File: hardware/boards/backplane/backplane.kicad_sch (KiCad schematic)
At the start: 0 parts

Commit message: Starrting to move things around
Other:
- added sheet Slot Connectors (backplane_slot_connectors.kicad_sch)
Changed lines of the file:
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@@
+	)
+	(sheet
+		(at 35.56 101.6)
+		(size 58.42 15.24)
+		(exclude_from_sim no)
+		(in_bom yes)
+		(on_board yes)
+		(dnp no)
+		(fields_autoplaced yes)
+		(stroke
+			(width 0.1524)
+			(type solid)
+		)
+		(fill
+			(color 0 0 0 0)
+		)
+		(property "Sheetname" "Slot Connectors"
+			(at 35.56 100.8884 0)
+			(show_name no)
+			(do_not_autoplace no)
+			(effects
+				(font
+					(size 1.27 1.27)
+				)
+				(justify left bottom)
+			)
+		)
+		(property "Sheetfile" "backplane_slot_connectors.kicad_sch"
+			(at 35.56 117.9446 0)
+			(show_name no)
+			(do_not_autoplace no)
+			(effects
+				(font
+					(size 1.27 1.27)
+				)
+				(justify left top)
+			)
+		)
 	)
 	(sheet

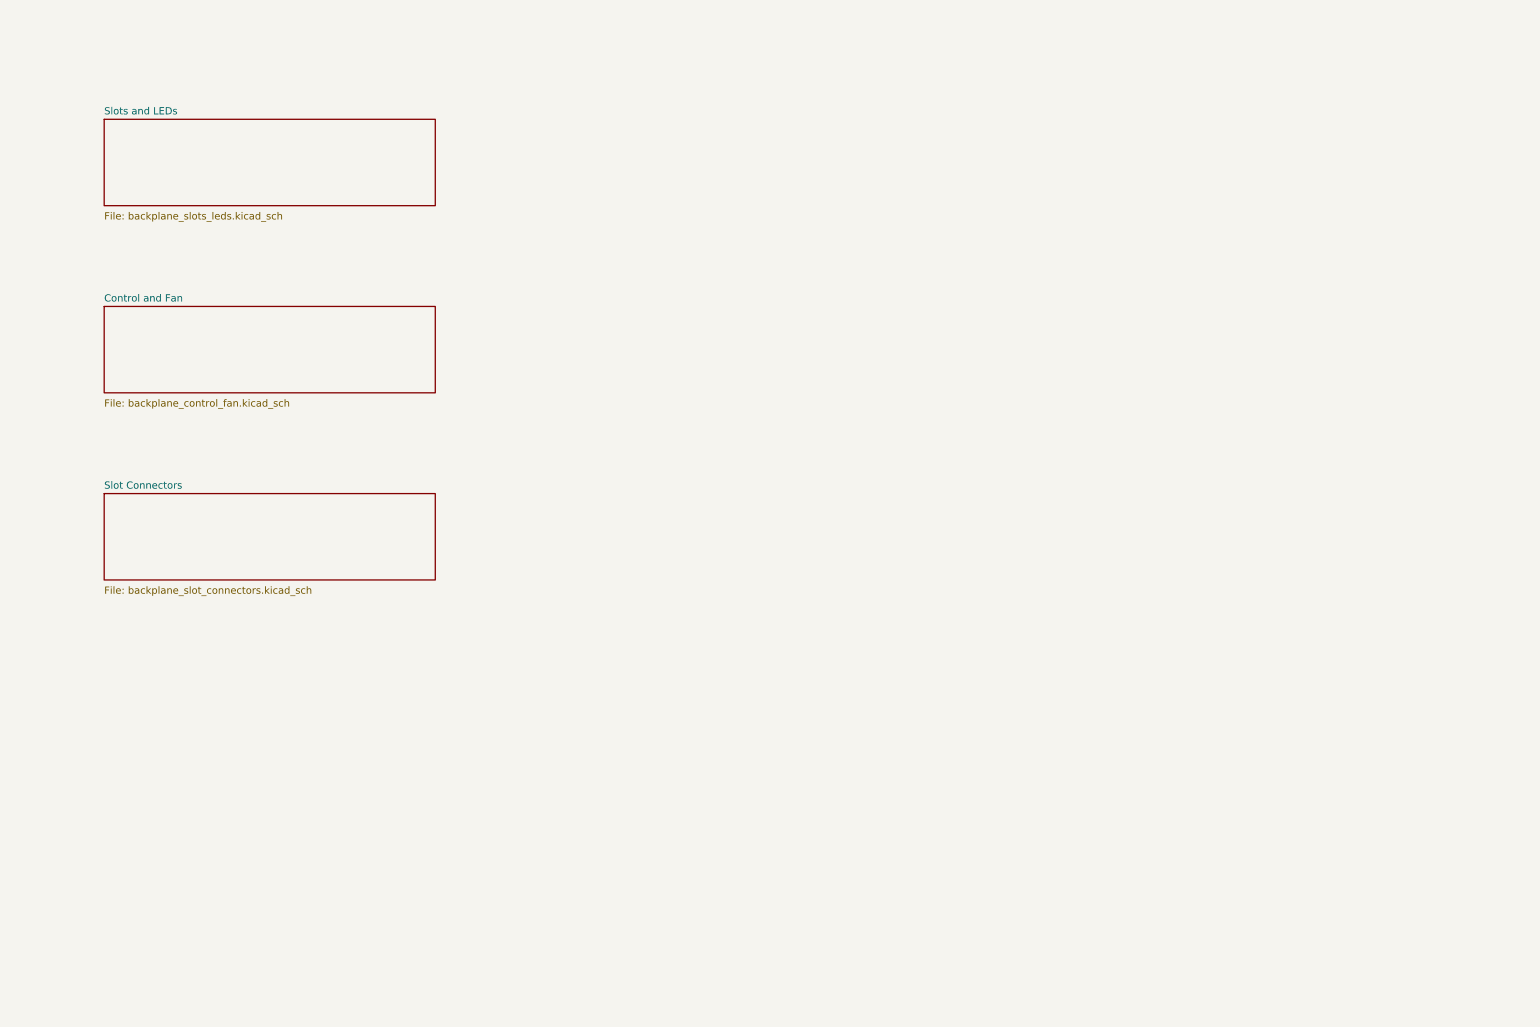
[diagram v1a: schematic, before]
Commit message: Clean up the backplane schematic
And start over with the PCB using a bit saner layout
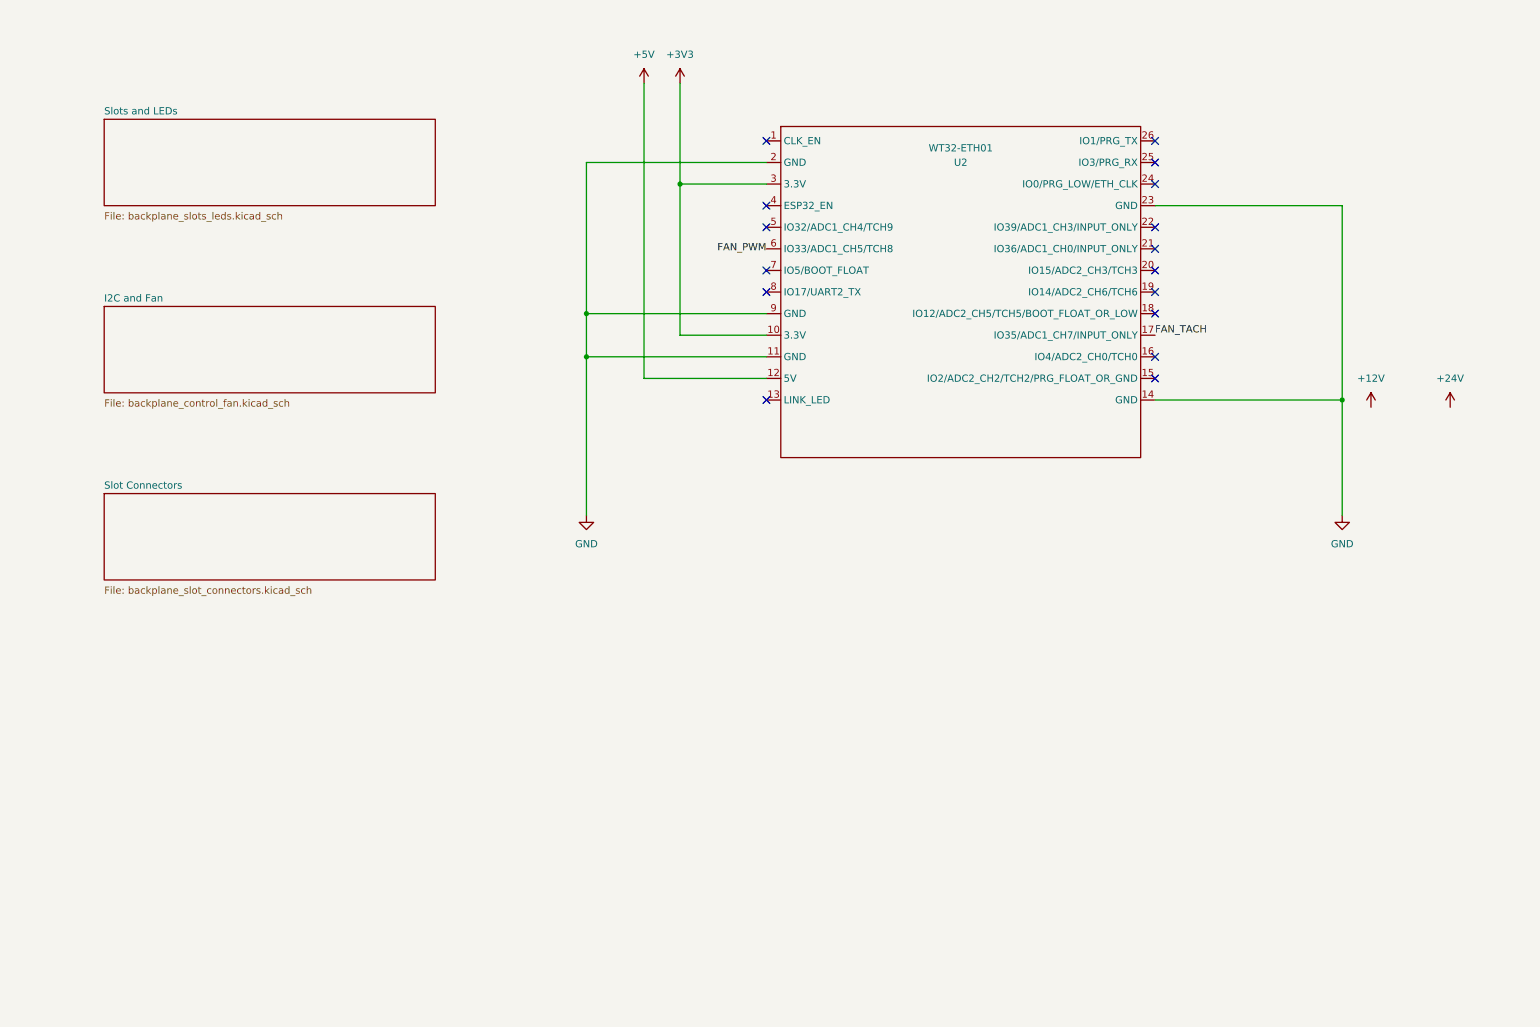
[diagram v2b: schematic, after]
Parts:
- added U2: WT32-ETH01, WT32-ETH01:WT32-ETH01, symbol WT32-ETH01:WT32-ETH01
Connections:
- new net +3V3: U2.10 (3.3V), U2.3 (3.3V)
- new net +5V: U2.12 (5V)
- new net FAN_PWM: U2.6 (IO33/ADC1_CH5/TCH8)
- new net FAN_TACH: U2.17 (IO35/ADC1_CH7/INPUT_ONLY)
- new net GND: U2.11 (GND), U2.14 (GND), U2.2 (GND), U2.23 (GND), U2.9 (GND)
- no-connect marks 0 -> 16
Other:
- sheet Control and Fan renamed I2C and Fan

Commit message: Split controller hardware from backplane
Add the central controller KiCad project for the WT32 and fan circuit, retain the I2C mux on the backplane, and update the system/interface documentation. Use C7519 arrays for interim slot I2C protection and record assembly-part alternatives.
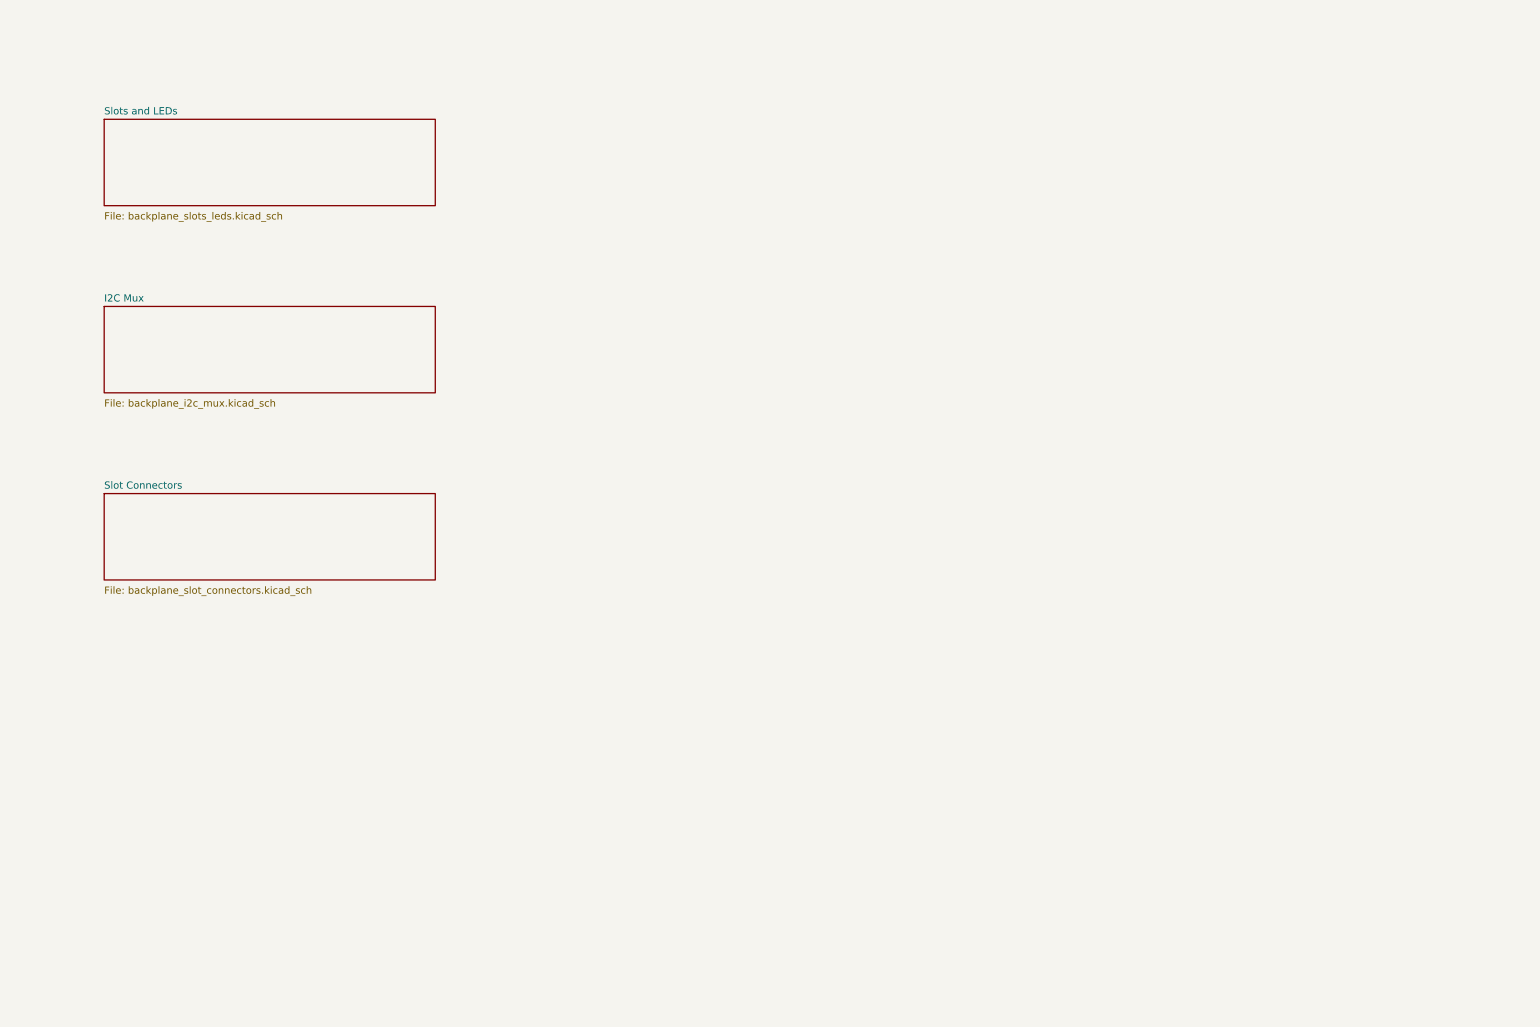
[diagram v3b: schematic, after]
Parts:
- removed U2: WT32-ETH01, WT32-ETH01:WT32-ETH01, symbol WT32-ETH01:WT32-ETH01
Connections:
- no-connect marks 16 -> 0
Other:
- sheet I2C and Fan renamed I2C Mux
- sheet I2C Mux: file backplane_control_fan.kicad_sch -> backplane_i2c_mux.kicad_sch

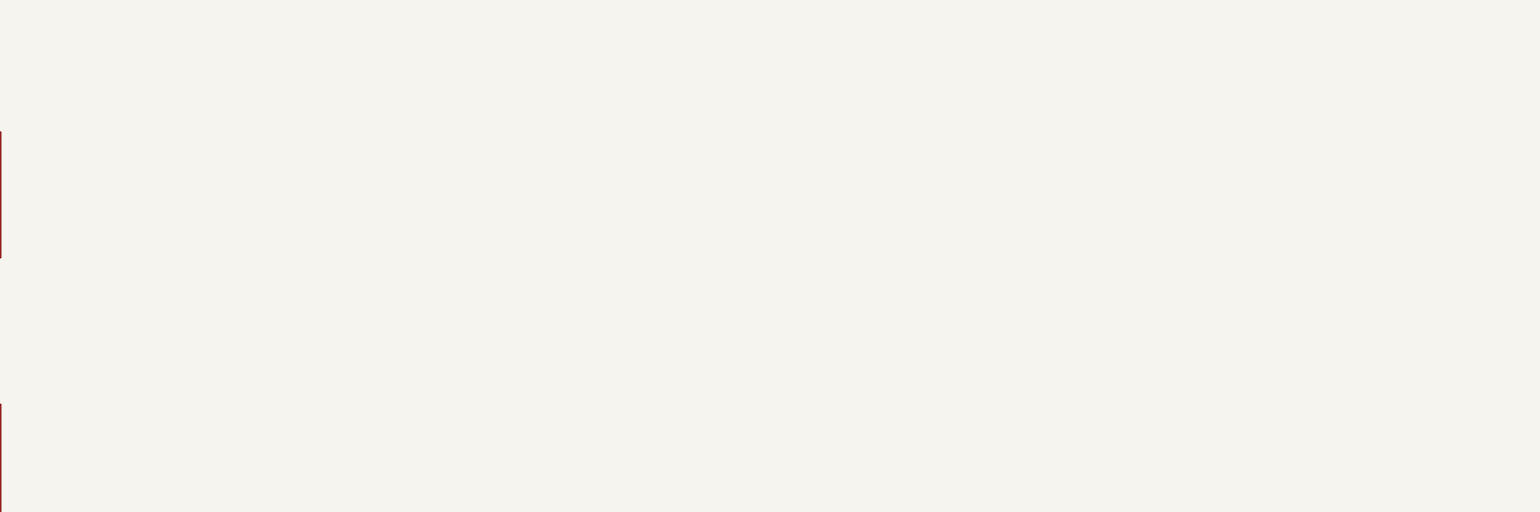
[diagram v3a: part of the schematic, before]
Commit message: Add adjustable DC-DC module to backplane
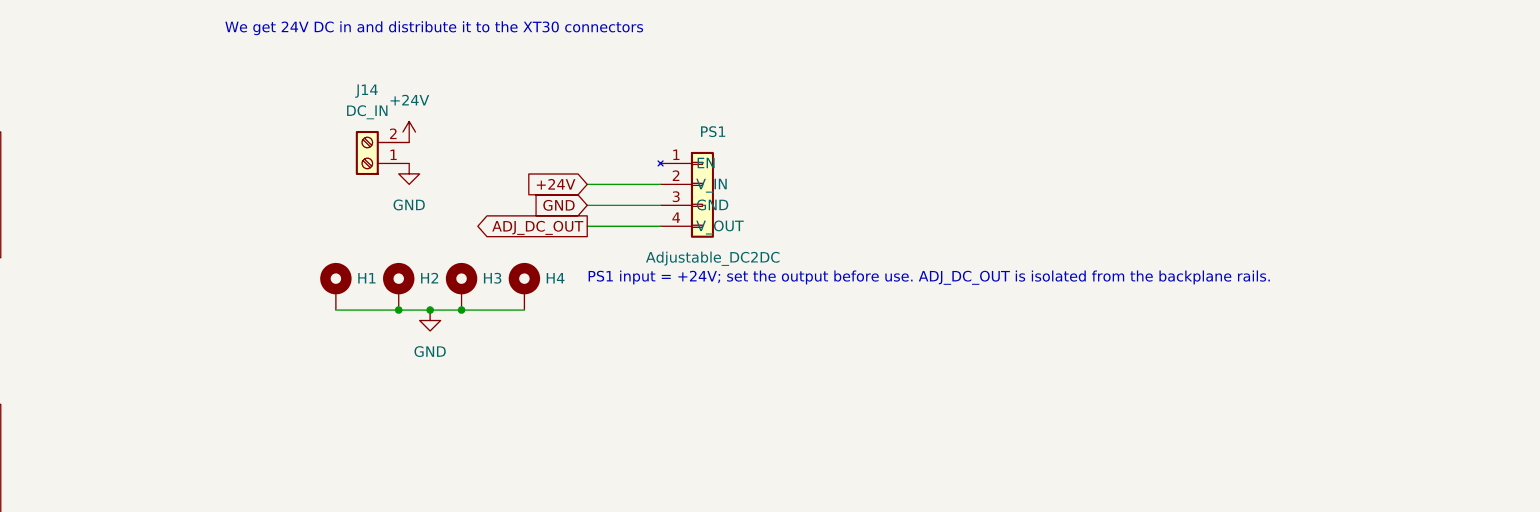
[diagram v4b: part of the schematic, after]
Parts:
- added H1, H2, H3, H4: MountingHole_Pad, MountingHole:MountingHole_3.2mm_M3_Pad_Via, symbol Mechanical:MountingHole_Pad
- added J14: DC_IN, mini-rack-power:DEGSON_DG135T-10.16-02P, symbol Connector:Screw_Terminal_01x02
- added PS1: Adjustable_DC2DC, mini-rack-power:Adjustable_DC2DC, symbol mini-rack-power:Adjustable_DC2DC
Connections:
- new net +24V: J14.2 (Pin_2), PS1.2 (V_IN)
- new net ADJ_DC_OUT: PS1.4 (V_OUT)
- new net GND: H1.1, H2.1, H3.1, H4.1, J14.1 (Pin_1), PS1.3 (GND)
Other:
- note added: "PS1 input = +24V; set the output before use. ADJ_DC_OUT is isolated from the backplane rails."
- note added: "We get 24V DC in and distribute it to the XT30 connectors"
